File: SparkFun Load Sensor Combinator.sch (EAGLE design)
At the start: 14 parts

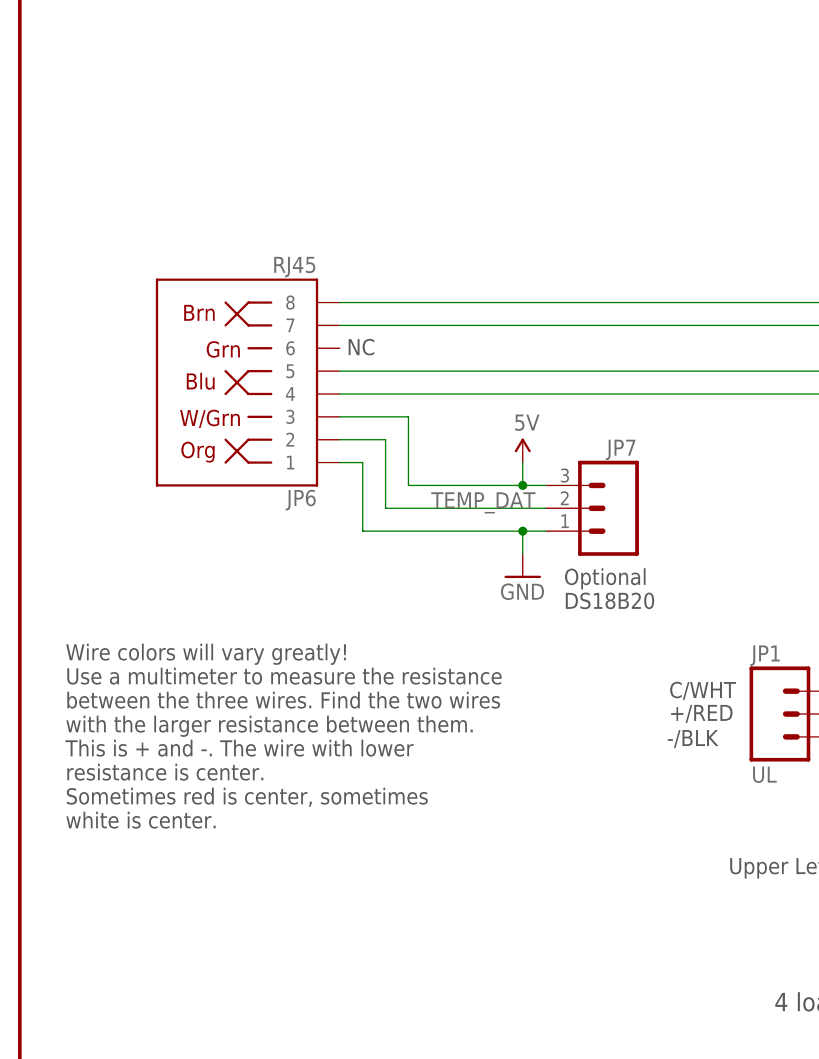
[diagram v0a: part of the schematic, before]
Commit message: Updates to readme with new photos and description
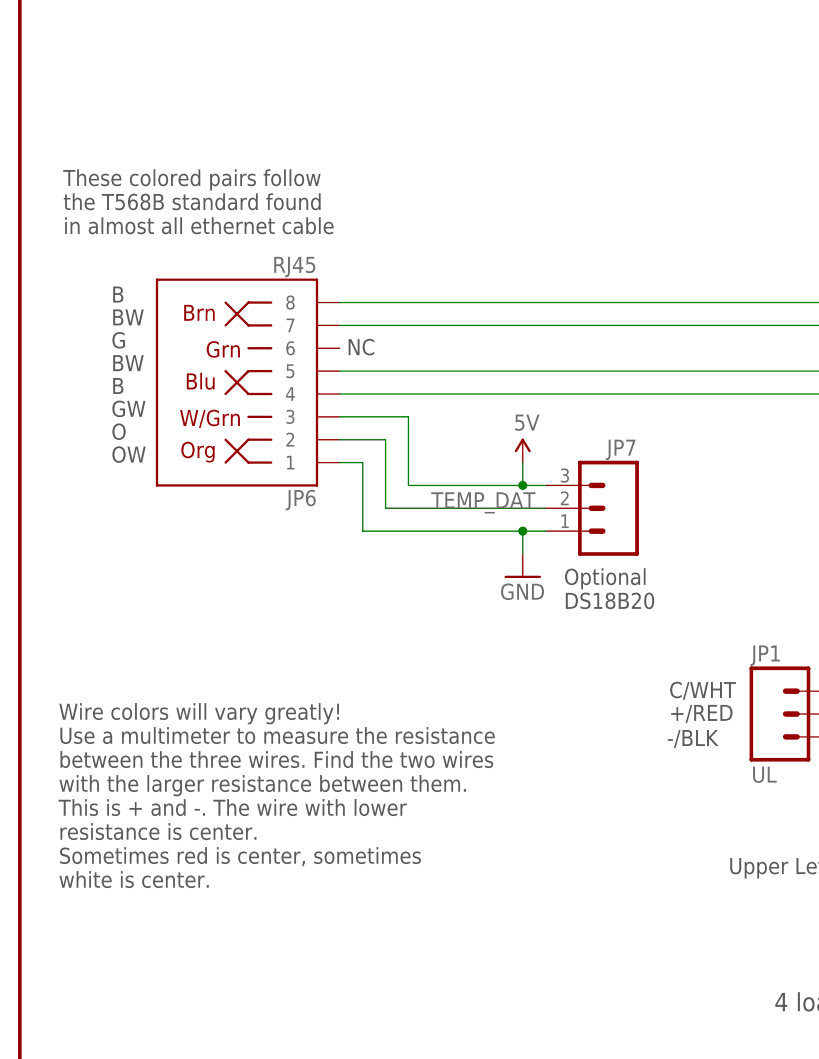
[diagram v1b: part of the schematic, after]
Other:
- note added: "B"
- note added: "BW"
- note added: "G"
- note added: "GW"
- note added: "O"
- note added: "OW"
- note added: "These colored pairs follow the T568B standard found in almost all ethernet cable"
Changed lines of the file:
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@@
 <?xml version="1.0" encoding="utf-8"?>
 <!DOCTYPE eagle SYSTEM "eagle.dtd">
-<eagle version="7.1.0">
+<eagle version="7.2.0">
 <drawing>
 <settings>
@@
 <text x="125.476" y="155.702" size="1.778" layer="97" rot="R90">White</text>
 <text x="128.016" y="155.702" size="1.778" layer="97" rot="R90">Green</text>
-<text x="5.08" y="73.66" size="1.778" layer="97">Wire colors will vary greatly\!
+<text x="4.318" y="67.056" size="1.778" layer="97">Wire colors will vary greatly\!
 Use a multimeter to measure the resistance
 between the three wires. Find the two wires
@@
 Sometimes red is center, sometimes
 white is center.</text>
+<text x="4.826" y="139.7" size="1.778" layer="97">These colored pairs follow
+the T568B standard found
+in almost all ethernet cable</text>
+<text x="10.16" y="129.54" size="1.778" layer="97">BW</text>
+<text x="10.16" y="132.08" size="1.778" layer="97">B</text>
+<text x="10.16" y="127" size="1.778" layer="97">G</text>
+<text x="10.16" y="121.92" size="1.778" layer="97">B</text>
+<text x="10.16" y="124.46" size="1.778" layer="97">BW</text>
+<text x="10.16" y="119.38" size="1.778" layer="97">GW</text>
+<text x="10.16" y="116.84" size="1.778" layer="97">O</text>
+<text x="10.16" y="114.3" size="1.778" layer="97">OW</text>
 </plain>
 <instances>
